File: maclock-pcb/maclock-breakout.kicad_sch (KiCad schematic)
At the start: 19 parts, among them J1 BM02B-SRSS-TB(LF)(SN), J2 BM04B-SRSS-TB(LF)(SN), J3 B2B-ZR(LF)(SN), SW1 TSB001A3518A, SW2 TSB001A3518A, U1 PAM8302AASCR

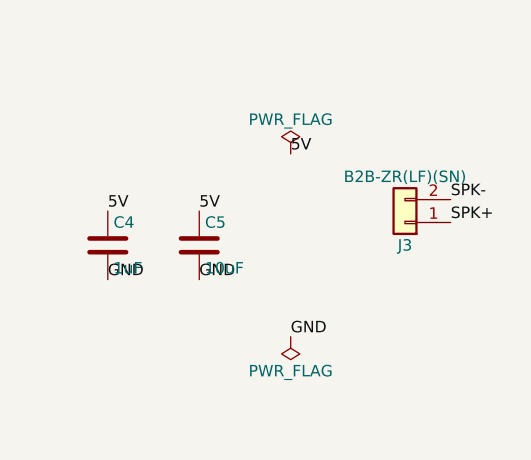
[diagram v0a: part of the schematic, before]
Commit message: J3: JST PH 2.0 mm speaker connector plus two bare-lead solder pads
Hobby 8 ohm 1 W speakers (Adafruit, Pimoroni, SparkFun) ship with a JST PH
2.0 mm plug, so J3 moves from ZH 1.5 mm to B2B-PH-K-S (C131337). For
speakers with bare leads, the new project footprint
maclock:JST_PH_B2B-PH-K_1x02_P2.00mm_Vertical_SolderPads adds two 2.54 mm
through-hole pads (1.7 mm ring, 1.0 mm hole) beside the housing that
duplicate pin 1 (+) and pin 2 (-). Keeping them inside the one footprint
means one BOM line and no dummy part to mark DNP.

Pin 1 stays at (137.75, 101.25); the SPK- leg now ends on the PH pin 2 at
x=135.75 and continues along the board edge to the far solder pad. +/- silk
added over the pads. ERC 0, DRC 0 errors / 0 unconnected (same two
pre-existing warnings). Speaker spec in the READMEs: 8 ohm, 1 W, 28-40 mm,
PH plug or bare leads.
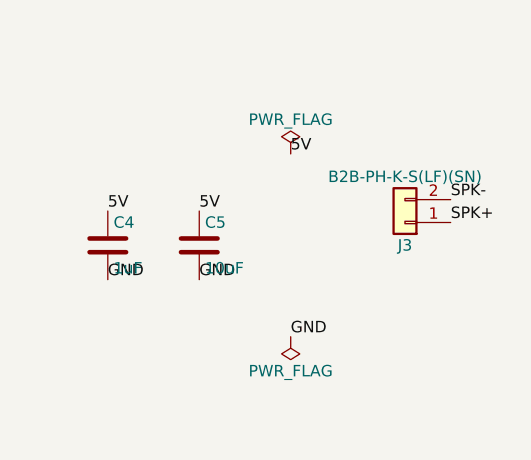
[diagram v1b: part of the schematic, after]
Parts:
- J3: value B2B-ZR(LF)(SN) -> B2B-PH-K-S(LF)(SN); footprint Connector_JST:JST_ZH_B2B-ZR_1x02_P1.50mm_Vertical -> maclock:JST_PH_B2B-PH-K_1x02_P2.00mm_Vertical_SolderPads; LCSC C158011 -> C131337
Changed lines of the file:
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@@
 			)
 		)
-		(property "Value" "B2B-ZR(LF)(SN)"
+		(property "Value" "B2B-PH-K-S(LF)(SN)"
 			(at 363.22 66.04 0)
 			(effects
@@
 			)
 		)
-		(property "Footprint" "Connector_JST:JST_ZH_B2B-ZR_1x02_P1.50mm_Vertical"
+		(property "Footprint" "maclock:JST_PH_B2B-PH-K_1x02_P2.00mm_Vertical_SolderPads"
 			(at 363.22 71.12 0)
 			(hide yes)
@@
 			)
 		)
-		(property "LCSC" "C158011"
+		(property "LCSC" "C131337"
 			(at 363.22 71.12 0)
 			(hide yes)

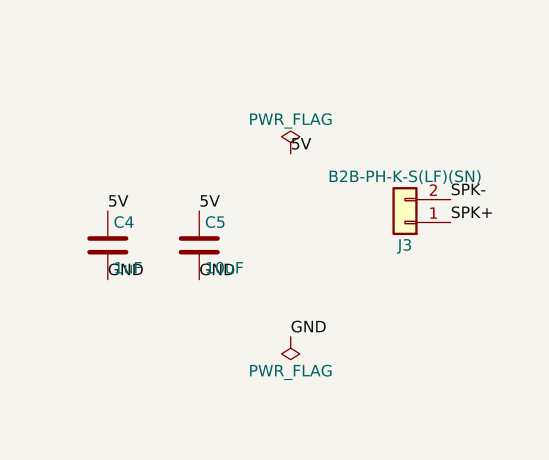
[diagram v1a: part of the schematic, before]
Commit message: Layout pass: SMD PH speaker connector, no solder pads, connectors re-placed
Hand layout in the PCB editor: J3 becomes the SMD JST PH B2B-PH-SM4-TB
(C160352) standing between the amp and the Speaker silk, the two bare-lead
solder pads and their project footprint are dropped, J1/J2 sit with their
solder tails toward the board edge (intentional), and the 5V / 5V_IN runs
are redrawn at 0.6 mm.

Fixes on top of that: a GND stitching via at (128.32, 94.03) landed 0.1 mm
from the ENC_A track and shorted the dial's A line to ground, so it is
removed (seventeen other stitching vias remain, 0 unconnected). The
schematic's J3 value, footprint and LCSC fields now match the board.
READMEs updated: J3 row, speaker row, all-SMD assembly note.
ERC 0, DRC 0 errors / 0 unconnected, parity clean apart from the usual
NC-pin notes.
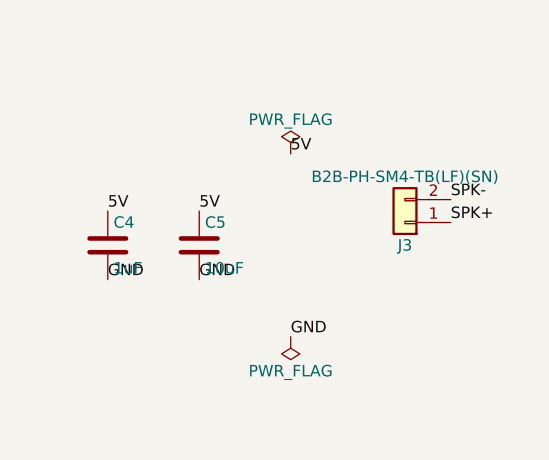
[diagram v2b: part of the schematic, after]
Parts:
- J3: value B2B-PH-K-S(LF)(SN) -> B2B-PH-SM4-TB(LF)(SN); footprint maclock:JST_PH_B2B-PH-K_1x02_P2.00mm_Vertical_SolderPads -> Connector_JST:JST_PH_B2B-PH-SM4-TB_1x02-1MP_P2.00mm_Vertical; LCSC C131337 -> C160352
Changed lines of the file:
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@@
 			)
 		)
-		(property "Value" "B2B-PH-K-S(LF)(SN)"
+		(property "Value" "B2B-PH-SM4-TB(LF)(SN)"
 			(at 363.22 66.04 0)
 			(effects
@@
 			)
 		)
-		(property "Footprint" "maclock:JST_PH_B2B-PH-K_1x02_P2.00mm_Vertical_SolderPads"
+		(property "Footprint" "Connector_JST:JST_PH_B2B-PH-SM4-TB_1x02-1MP_P2.00mm_Vertical"
 			(at 363.22 71.12 0)
 			(hide yes)
@@
 			)
 		)
-		(property "LCSC" "C131337"
+		(property "LCSC" "C160352"
 			(at 363.22 71.12 0)
 			(hide yes)

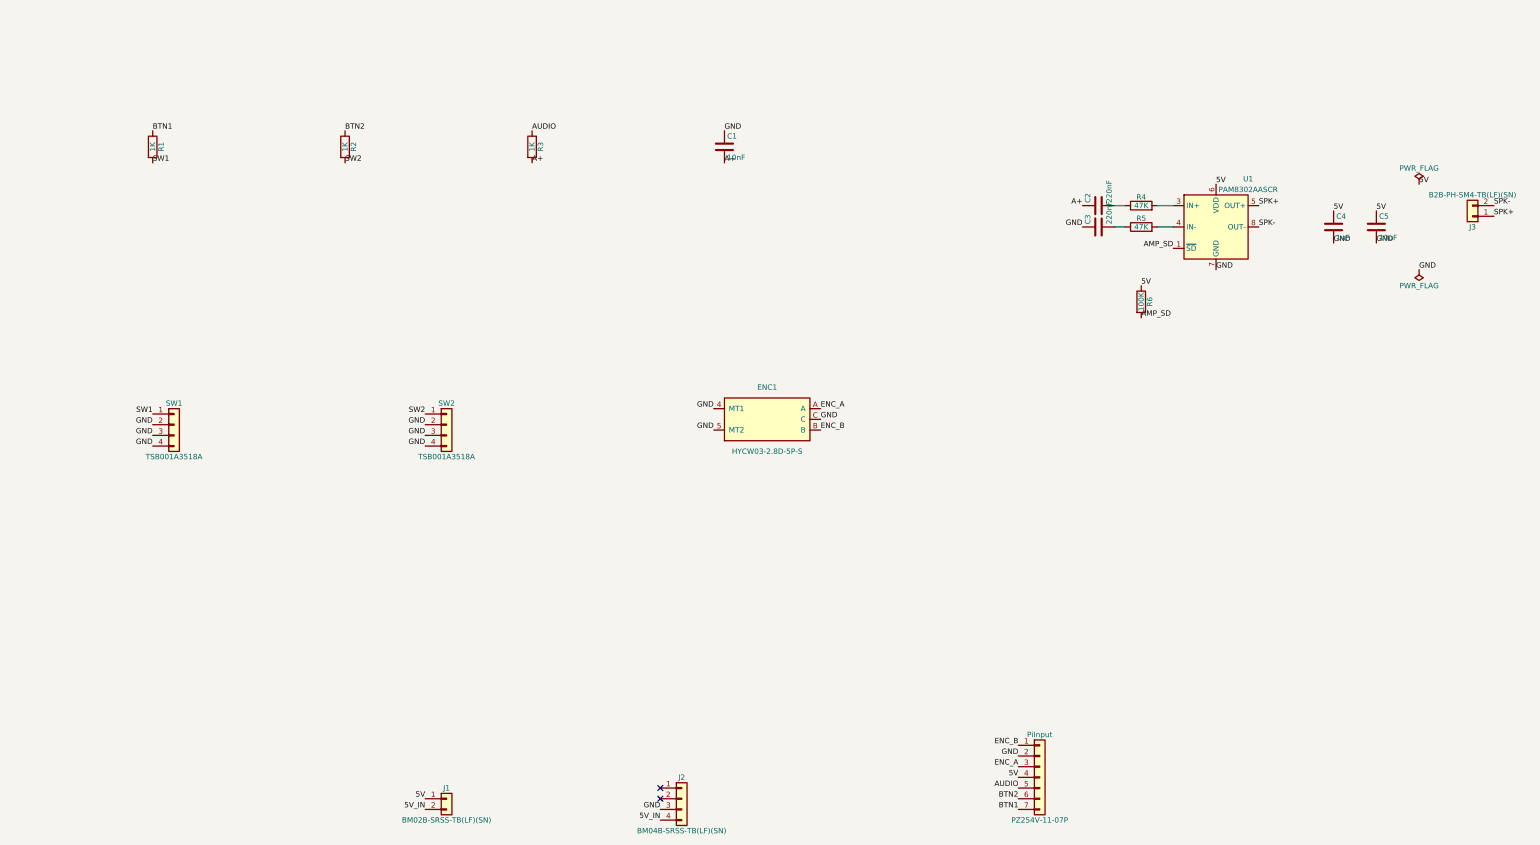
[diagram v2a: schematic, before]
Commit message: PCB rev 2026.10: E8E8 dial, LCSC switches, PicoBlade connectors, clean schematic
Connectors: J1, J2 and J3 are Molex PicoBlade 1.25 mm (53398-0271 /
53398-0471), the pitch of the Maclock's own power, switch and speaker plugs;
the JST SH/PH parts on the first boards did not take them. The three now share
one row, 0.6 mm closer to the bottom edge, which also moves ENC1's rear post
hole out of J3's courtyard.

ENC1 is the F-Switch E8E8-3.2C60-9B34 (1.74 mm hex bore; the HYCW03's 1.78 mm
was too loose for the dial), sold by dicomon and not stocked at LCSC. Its
footprint is the proto board's Dial land with the origin on the bore, its
outline and 3D model (build123d STEP) are measured from a real part, and the
silkscreen shows the body and the 21 mm wheel's clearance. The symbol is KiCad's
encoder with an MP pin for the solder tabs. ENC_A/ENC_B are routed on F.Cu
straight to the pad centres.

SW1/SW2 use LCSC's own TSB001A3518A symbol, footprint and STEP (C2888448), in a
new `lcsc` project library imported with easyeda2kicad. Only the conversion
artefacts are fixed: NPTH peg holes, no outline stroke on the bracket pads (it
made them fail edge clearance), passive pins, one closed courtyard. The one-off
switch footprint and the HYCW03 footprint are gone; `maclock` now holds ENC1
only.

The schematic is rebuilt as one A4 sheet in functional blocks (Raspberry Pi,
power, buttons, dial, audio amplifier) with power symbols, notes and a filled
title block. Every part carries Manufacturer, MPN and LCSC fields, and ENC1 a
dicomon Supplier and link, so any exported BOM names the source. PiInput is J4.
Board nets and fields follow (GND, +5V, no-connect nets): schematic parity 0.

Also: C4/C5 ground pads get thermal reliefs (C1/C3 sit in pour too broken up to
form spokes and stay solid); the OSHW logo is removed, since the CC BY-NC-SA
licence is outside the OSHW definition; the board has a title block.
production/ (kicad-cli fab outputs) and the Fabrication Toolkit's options file
are 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
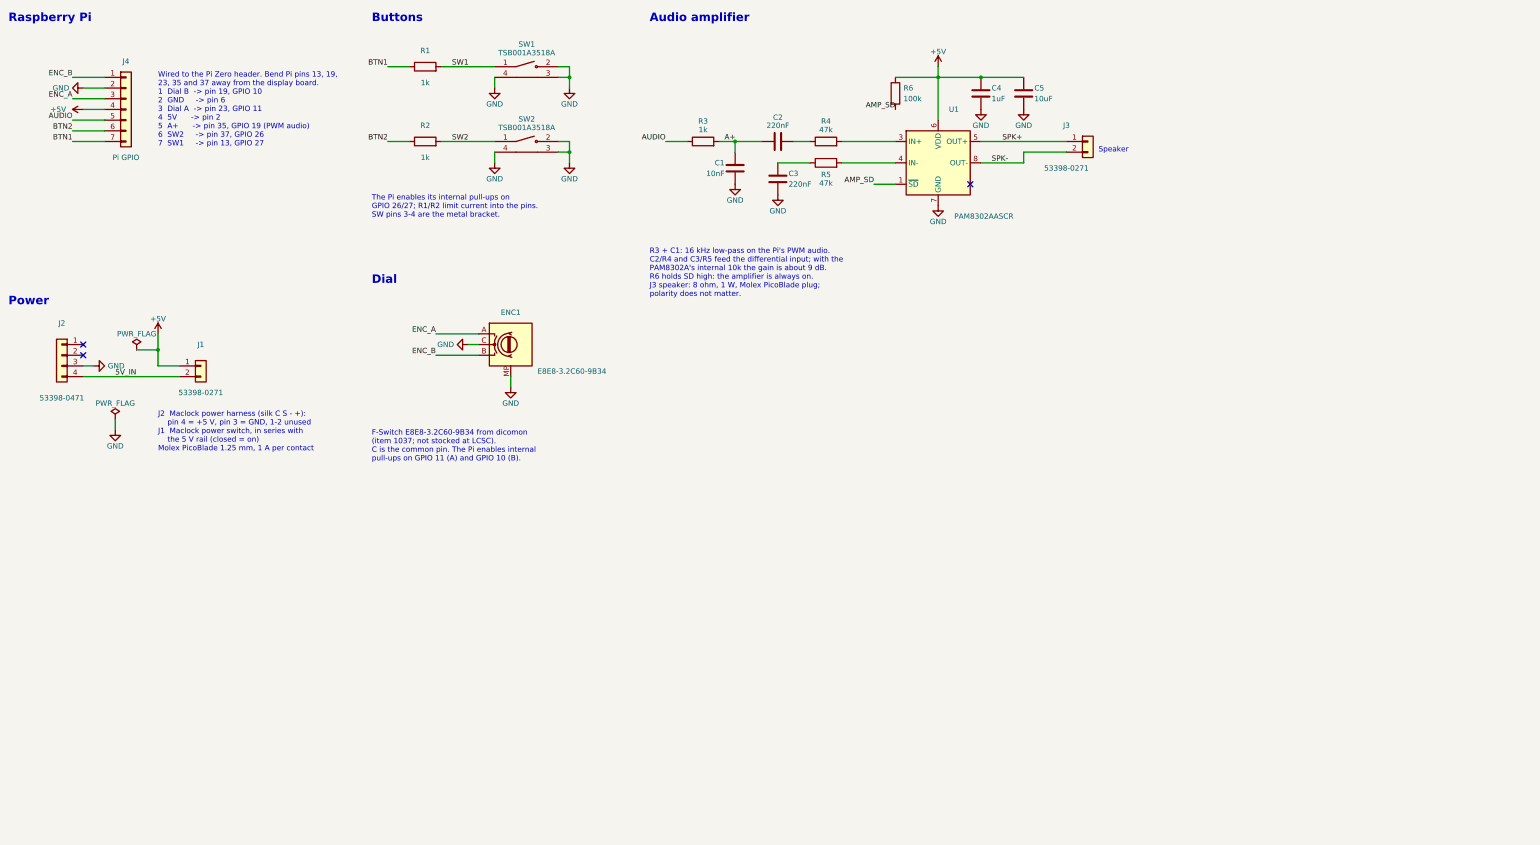
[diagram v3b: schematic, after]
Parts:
- C1: MPN (none) -> 0603B103K500NT; Manufacturer (none) -> FH (Guangdong Fenghua)
- C2, C3: MPN (none) -> CL10B224KA8NNNC; Manufacturer (none) -> Samsung Electro-Mechanics
- C4: MPN (none) -> CL10A105KB8NNNC; Manufacturer (none) -> Samsung Electro-Mechanics
- C5: MPN (none) -> CL21A106KAYNNNE; Manufacturer (none) -> Samsung Electro-Mechanics
- ENC1: value HYCW03-2.8D-5P-S -> E8E8-3.2C60-9B34; footprint maclock:RotaryEncoder_HYCW03-2.8D-5P-S_SMD -> maclock:RotaryEncoder_E8E8-3.2C60-9B34_SMD; symbol maclock:RotaryEncoder_HYCW03-2.8D-5P-S -> maclock:RotaryEncoder_E8E8-3.2C60-9B34; LCSC C55218995 -> (none); MPN (none) -> E8E8-3.2C60-9B34; Manufacturer (none) -> F-Switch; Supplier (none) -> dicomon; Supplier Link (none) -> https://www.dicomon.com/index.php?ctl=Product&met=detail&it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
- J1: value BM02B-SRSS-TB(LF)(SN) -> 53398-0271; footprint Connector_JST:JST_SH_BM02B-SRSS-TB_1x02-1MP_P1.00mm_Vertical -> Connector_Molex:Molex_PicoBlade_53398-0271_1x02-1MP_P1.25mm_Vertical; LCSC C160388 -> C122410; MPN (none) -> 53398-0271; Manufacturer (none) -> Molex
- J2: value BM04B-SRSS-TB(LF)(SN) -> 53398-0471; footprint Connector_JST:JST_SH_BM04B-SRSS-TB_1x04-1MP_P1.00mm_Vertical -> Connector_Molex:Molex_PicoBlade_53398-0471_1x04-1MP_P1.25mm_Vertical; LCSC C160390 -> C17617036; MPN (none) -> 53398-0471; Manufacturer (none) -> Molex
- J3: value B2B-PH-SM4-TB(LF)(SN) -> 53398-0271; footprint Connector_JST:JST_PH_B2B-PH-SM4-TB_1x02-1MP_P2.00mm_Vertical -> Connector_Molex:Molex_PicoBlade_53398-0271_1x02-1MP_P1.25mm_Vertical; LCSC C160352 -> C122410; MPN (none) -> 53398-0271; Manufacturer (none) -> Molex
- J4: renamed from PiInput; value PZ254V-11-07P -> Pi GPIO; MPN (none) -> PZ254V-11-07P; Manufacturer (none) -> XFCN
- R1, R2, R3: value 1K -> 1k; MPN (none) -> 0402WGF1001TCE; Manufacturer (none) -> UNI-ROYAL
- R4, R5: value 47K -> 47k; MPN (none) -> 0402WGF4702TCE; Manufacturer (none) -> UNI-ROYAL
- R6: value 100K -> 100k; MPN (none) -> 0402WGF1003TCE; Manufacturer (none) -> UNI-ROYAL
- SW1, SW2: footprint maclock:SW_TSB001_7.7x3.55_SideSMD -> lcsc:SW-SMD_TSB001XXXX; symbol Connector_Generic:Conn_01x04 -> lcsc:TSB001A3518A; MPN (none) -> TSB001A3518A; Manufacturer (none) -> BZCN
- U1: MPN (none) -> PAM8302AASCR; Manufacturer (none) -> Diodes Incorporated
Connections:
- net GND: now also ENC1.MP; no longer ENC1.4 (MT1), ENC1.5 (MT2)
- net 5V renamed +5V
- no-connect marks 2 -> 3
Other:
- note added: "Audio amplifier"
- note added: "Buttons"
- note added: "Dial"
- note added: "F-Switch E8E8-3.2C60-9B34 from dicomon (item 1037; not stocked at LCSC). C is the common pin. The Pi enables internal pull-ups on GPIO 11 (A) and GPIO 10 (B)."
- note added: "J2 Maclock power harness (silk C S - +): pin 4 = +5 V, pin 3 = GND, 1-2 unused J1 Maclock power switch, in series with the 5 V rail (closed = on) Molex PicoBlade 1.25 mm, 1 A per contact"
- note added: "Power"
- note added: "R3 + C1: 16 kHz low-pass on the Pi's PWM audio. C2/R4 and C3/R5 feed the differential input; with the PAM8302A's internal 10k the gain is about 9 dB. R6 holds SD high: the amplifier is always on. J3 speaker: 8 ohm, 1 W, Molex PicoBlade plug; polarity does not matter."
- note added: "Raspberry Pi"
- note added: "Speaker"
- note added: "The Pi enables its internal pull-ups on GPIO 26/27; R1/R2 limit current into the pins. SW pins 3-4 are the metal bracket."
- note added: "Wired to the Pi Zero header. Bend Pi pins 13, 19, 23, 35 and 37 away from the display board. 1 Dial B -> pin 19, GPIO 10 2 GND -> pin 6 3 Dial A -> pin 23, GPIO 11 4 5V -> pin 2 5 A+ -> pin 35, GPIO 19 (PWM audio) 6 SW2 -> pin 37, GPIO 26 7 SW1 -> pin 13, GPIO 27"
- company: (none) -> Wells Workshop
- title: (none) -> Macintosh Mini breakout
- moved on the sheet: C1, C2, C3, C4, C5, J1, J2, J3, J4, R1, R2, R3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

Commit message: Breakout: put back the Switch / Power / Speaker labels and J2's + / -
Rev 2026.10's field cleanup deleted the board-only "Label" field that
named J1-J3 on the back silk, leaving three identical PicoBlade sockets
and no polarity mark on the power input. The labels are back above the
connectors, now as a "Label" field on the schematic symbols too, so an
Update PCB from Schematic can't strip them again. "Speaker" sits 0.3 mm
right of centre to clear ENC1's peg hole. J2 gets + over pin 4 (5V) and
- over pin 3 (GND), as before.
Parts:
- J1: Label (none) -> Switch
- J2: Label (none) -> Power
- J3: Label (none) -> Speaker
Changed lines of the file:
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@@
+			)
+		)
+		(property "Label" "Power"
+			(at 27.94 104.14 0)
+			(hide yes)
+			(effects
+				(font
+					(size 1.27 1.27)
+				)
 			)
 		)
@@
 			)
 		)
+		(property "Label" "Switch"
+			(at 60.96 106.68 0)
+			(hide yes)
+			(effects
+				(font
+					(size 1.27 1.27)
+				)
+			)
+		)
 		(pin "1"
 		)
@@
 			(at 271.78 53.34 0)
 			(hide yes)
+			(effects
+				(font
+					(size 1.27 1.27)
+				)
+			)
+		)
+		(property "Label" "Speaker"
+			(at 271.78 53.34 0)
+			(hide yes)
